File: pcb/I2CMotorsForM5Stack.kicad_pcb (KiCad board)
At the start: 2 copper layers, 54 x 54 mm, 26 parts, among them J1 free_holes, J2 Conn_01x04, J3 Conn_01x06, U1 TB6612FNG, U2 ATmega328P-MU

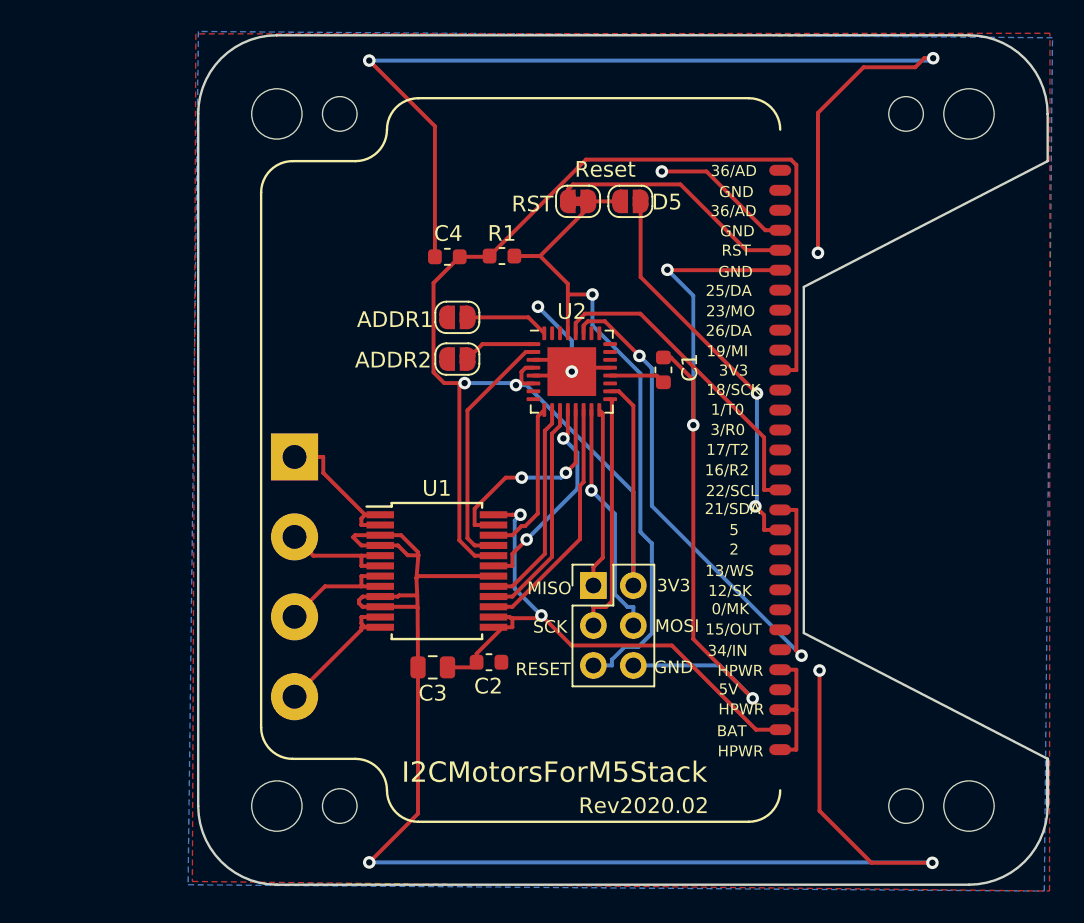
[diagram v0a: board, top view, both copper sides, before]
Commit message: Put terminal mount out side of m5stack zone
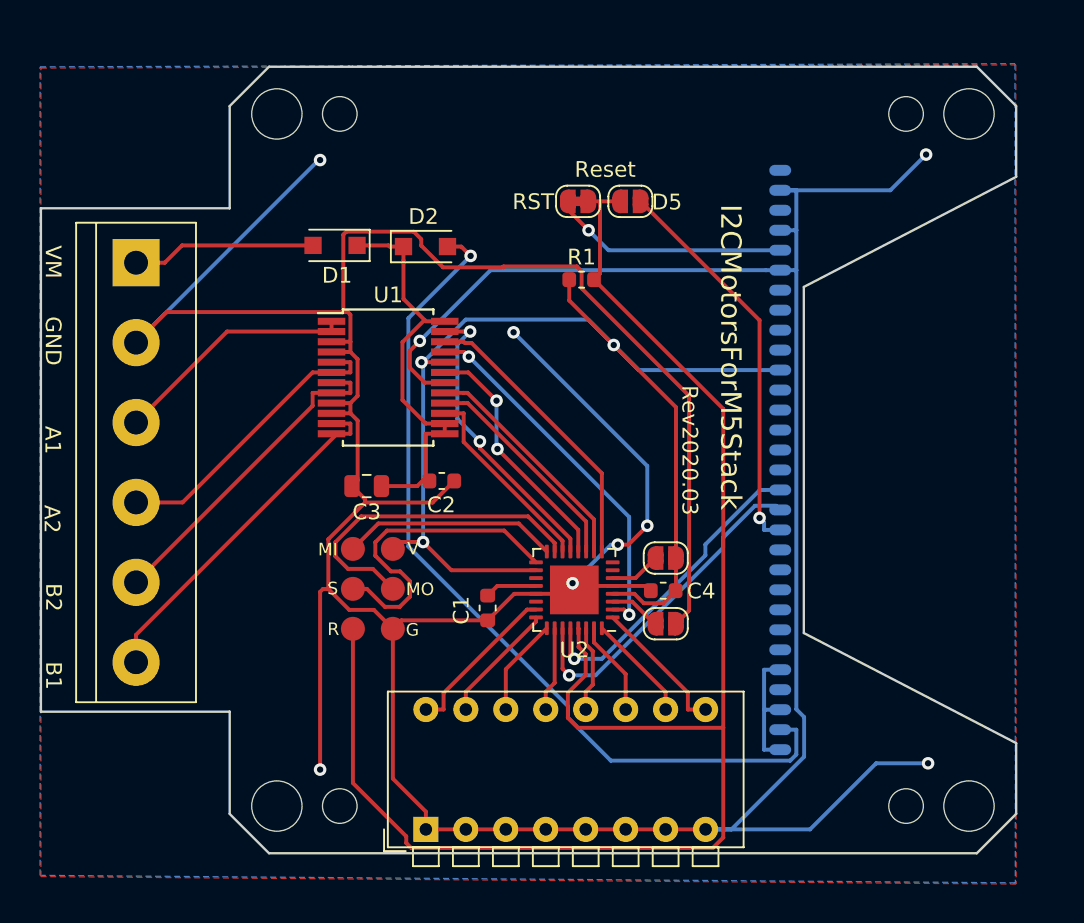
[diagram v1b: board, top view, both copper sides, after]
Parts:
- removed J2: Conn_01x04, TerminalBlock:TerminalBlock_bornier-4_P5.08mm
- removed corner1, corner2, corner3, corner4: outer_corner, footprints:outer_corner
- added D1: D, Diode_SMD:D_SOD-123F, F.Cu at (106.7, 61.4)
- added D2: D, Diode_SMD:D_SOD-123F, F.Cu at (112.4, 61.4)
- added J4: Conn_01x06, TerminalBlock:TerminalBlock_bornier-6_P5.08mm, F.Cu at (94.0, 62.5)
- added SW1: SW_DIP_x08, Button_Switch_THT:SW_DIP_SPSTx08_Piano_CTS_Series194-8MSTN_W7.62mm_P2.54mm, F.Cu at (112.5, 98.5)
- J1: moved to B.Cu
- J3: footprint Connector_PinHeader_2.54mm:PinHeader_2x03_P2.54mm_Vertical -> footprints:2x03_P2.54mm_Pads
- JP3, JP4: value Jumper_NO_Small -> NC
- U2: value ATmega328P-MU -> ATmega328PB-MU
- moved C4 25.3 mm to (127.6, 83.3)
- moved JP3 23.6 mm to (127.7, 85.4)
- moved C1 18.8 mm to (116.4, 84.4), turned to 270 degrees
- moved JP4 18.3 mm to (127.7, 81.2)
- moved J3 14.0 mm to (109.1, 83.2)
- moved U2 13.9 mm to (121.9, 83.3), turned to 180 degrees
- moved U1 12.7 mm to (110.1, 69.8)
- moved C3 12.3 mm to (108.7, 76.7)
- moved C2 11.9 mm to (113.5, 76.3)
- moved R1 5.28 mm to (122.4, 63.5)
- turned J1 to 180 degrees
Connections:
- C2 pad 1: +BATT -> Net-(C2-Pad1)
- C3 pad 1: +BATT -> Net-(C2-Pad1)
- JP3 pad 1: /ADDR1 -> GND
- JP3 pad 2: GND -> Net-(JP3-Pad2)
- JP4 pad 1: /ADDR2 -> +3V3
- JP4 pad 2: GND -> Net-(JP4-Pad2)
- U1 pad 13: +BATT -> Net-(C2-Pad1)
- U1 pad 14: +BATT -> Net-(C2-Pad1)
- U1 pad 24: +BATT -> Net-(C2-Pad1)
- U2 pad 1: /ADDR2 -> /ADDR8
- U2 pad 23: Net-(U2-Pad23) -> /ADDR1
- U2 pad 24: Net-(U2-Pad24) -> /ADDR2
- U2 pad 25: Net-(U2-Pad25) -> /ADDR3
- U2 pad 26: Net-(U2-Pad26) -> /ADDR4
- U2 pad 3: GND -> Net-(JP3-Pad2)
- U2 pad 30: Net-(U2-Pad30) -> /ADDR5
- U2 pad 31: Net-(U2-Pad31) -> /ADDR6
- U2 pad 32: /ADDR1 -> /ADDR7
- U2 pad 6: +3V3 -> Net-(JP4-Pad2)
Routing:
- net GND: track 236.6 -> 300.2 mm, vias 12 -> 9
- net /SPI_RESET: track 43.5 -> 98.1 mm, vias 1 -> 0
- net Net-(C2-Pad1): track 0.00 -> 26.5 mm
- net +3V3: track 96.6 -> 75.4 mm, vias 2 -> 3
- net +BATT: track 37.0 -> 55.3 mm, vias 2 -> 1
- net /21: track 38.8 -> 21.5 mm, vias 2 -> 1
- net /B1: track 9.32 -> 22.9 mm
- net /B2: track 8.10 -> 20.9 mm
- net VCC: track 0.00 -> 11.7 mm
- net /A2: track 7.80 -> 18.9 mm
- net /ADDR8: track 0.00 -> 8.96 mm
- net /AIN2: track 10.1 -> 18.4 mm
- net /AIN1: track 15.7 -> 23.5 mm, vias 0 -> 2
- net /ADDR7: track 0.00 -> 6.85 mm
- net /MOSI: track 15.0 -> 21.3 mm, vias 1 -> 0
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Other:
- board size 54 x 54 mm -> 62 x 50 mm
- board text added: "Please put components on front side."
- board text added: "Rev2020.03"
- board text added: "VM"
- board text removed: "ADDR1"
- board text removed: "ADDR2"
- board text removed: "MISO"
- board text removed: "MOSI"
- board text removed: "Please put components on back side."
- board text removed: "RESET"
- board text removed: "Rev2020.02"
- board text removed: "SCK"

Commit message: Use rounded corner
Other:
- board size 62 x 50 mm -> 60 x 50 mm
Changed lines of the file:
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@@
   (general
     (thickness 1.6)
-    (drawings 59)
+    (drawings 67)
     (tracks 346)
     (zones 0)
@@
     (tags D_SOD-123F)
     (attr smd)
-    (fp_text reference D1 (at -0.127 -1.905) (layer F.SilkS)
+    (fp_text reference D1 (at -0.0248 1.875) (layer F.SilkS)
       (effects (font (size 1 1) (thickness 0.15)))
     )
@@
     )
   )
-  (gr_line (start 100 91) (end 100 97.5) (layer Edge.Cuts) (width 0.15))
-  (gr_line (start 88 91) (end 100 91) (layer Edge.Cuts) (width 0.15))
-  (gr_line (start 88 59) (end 88 91) (layer Edge.Cuts) (width 0.15))
-  (gr_line (start 100 59) (end 88 59) (layer Edge.Cuts) (width 0.15))
-  (gr_text VM (at 88.7738 62.4082 270) (layer F.SilkS)
+  (gr_text B1 (at 90.8988 87.9082 270) (layer B.SilkS)
+    (effects (font (size 1 1) (thickness 0.15)) (justify mirror))
+  )
+  (gr_text B2 (at 90.7738 82.8082 270) (layer B.SilkS)
+    (effects (font (size 1 1) (thickness 0.15)) (justify mirror))
+  )
+  (gr_text A2 (at 90.8488 77.6832 270) (layer B.SilkS)
+    (effects (font (size 1 1) (thickness 0.15)) (justify mirror))
+  )
+  (gr_text A1 (at 90.8488 72.5332 270) (layer B.SilkS)
+    (effects (font (size 1 1) (thickness 0.15)) (justify mirror))
+  )
+  (gr_text GND (at 90.8488 67.5082 270) (layer B.SilkS)
+    (effects (font (size 1 1) (thickness 0.15)) (justify mirror))
+  )
+  (gr_text VM (at 90.8238 62.5082 270) (layer B.SilkS)
+    (effects (font (size 1 1) (thickness 0.15)) (justify mirror))
+  )
+  (gr_arc (start 92 93) (end 90 93) (angle -90) (layer Edge.Cuts) (width 0.15))
+  (gr_arc (start 92 57) (end 92 55) (angle -90) (layer Edge.Cuts) (width 0.15))
+  (gr_line (start 100 95) (end 100 97.5) (layer Edge.Cuts) (width 0.15))
+  (gr_line (start 92 95) (end 100 95) (layer Edge.Cuts) (width 0.15))
+  (gr_line (start 90 57) (end 90 93) (layer Edge.Cuts) (width 0.15))
+  (gr_line (start 100 55) (end 92 55) (layer Edge.Cuts) (width 0.15))
+  (gr_text VM (at 92.6738 55.8582 180) (layer F.SilkS)
     (effects (font (size 1 1) (thickness 0.15)))
   )
-  (gr_text GND (at 88.7738 67.4332 270) (layer F.SilkS)
+  (gr_text GND (at 93.0488 57.4082 180) (layer F.SilkS)
     (effects (font (size 1 1) (thickness 0.15)))
   )
@@
   (gr_line (start 102.5 100) (end 147.5 100) (layer Edge.Cuts) (width 0.15))
   (gr_line (start 100 97.5) (end 102.5 100) (layer Edge.Cuts) (width 0.15))
-  (gr_line (start 100 52.5) (end 100 59) (layer Edge.Cuts) (width 0.15))
+  (gr_line (start 100 52.5) (end 100 55) (layer Edge.Cuts) (width 0.15))
   (gr_line (start 102.5 50) (end 100 52.5) (layer Edge.Cuts) (width 0.15))
   (gr_line (start 147.5 50) (end 102.5 50) (layer Edge.Cuts) (width 0.15))
@@
     (effects (font (size 1 1) (thickness 0.15)))
   )
-  (gr_text B1 (at 88.7988 88.7082 270) (layer F.SilkS)
+  (gr_text B1 (at 92.2488 94.1582) (layer F.SilkS)
     (effects (font (size 1 1) (thickness 0.15)))
   )
-  (gr_text B2 (at 88.7988 83.7332 270) (layer F.SilkS)
+  (gr_text B2 (at 92.2488 92.7332) (layer F.SilkS)
     (effects (font (size 1 1) (thickness 0.15)))
   )
-  (gr_text A2 (at 88.6988 78.7582 270) (layer F.SilkS)
+  (gr_text A2 (at 92.3488 91.3082) (layer F.SilkS)
     (effects (font (size 1 1) (thickness 0.15)))
   )
-  (gr_text A1 (at 88.7488 73.7332 270) (layer F.SilkS)
+  (gr_text A1 (at 92.4488 58.9082 180) (layer F.SilkS)
     (effects (font (size 1 1) (thickness 0.15)))
   )
@@
     (polygon
       (pts
-        (xy 149.9988 101.9582) (xy 87.9988 101.4832) (xy 87.9988 50.0832) (xy 149.9738 49.8832)
+        (xy 149.9988 101.9582) (xy 87.3988 101.556437) (xy 87.3988 50.159963) (xy 149.9738 49.8832)
       )
     )
@@
     (polygon
       (pts
-        (xy 149.9488 101.8832) (xy 87.9488 101.4082) (xy 87.9488 50.0082) (xy 149.9238 49.8082)
+        (xy 149.9488 101.8832) (xy 87.5488 101.3082) (xy 87.5488 49.9082) (xy 149.9238 49.8082)
       )
     )

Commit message: Add diode to connect VM and GND
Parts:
- added D3: D, Diode_SMD:D_SOD-123F, F.Cu at (112.5, 57.6)
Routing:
- net GND: track 300.2 -> 311.0 mm
- net Net-(C2-Pad1): track 26.5 -> 30.3 mm
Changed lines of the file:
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@@
-(kicad_pcb (version 20171130) (host pcbnew 5.1.5-52549c5~84~ubuntu18.04.1)
+(kicad_pcb (version 20171130) (host pcbnew 5.1.5-52549c5~86~ubuntu18.04.1)
   (general
     (thickness 1.6)
     (drawings 67)
-    (tracks 346)
+    (tracks 356)
     (zones 0)
-    (modules 25)
+    (modules 26)
     (nets 59)
   )
@@
     (add_net VCC)
   )
+  (module Diode_SMD:D_SOD-123F (layer F.Cu)
+    (at 112.4738 57.6082)
+    (descr D_SOD-123F)
+    (tags D_SOD-123F)
+    (attr smd)
+    (fp_text reference D3 (at -0.127 -1.905) (layer F.SilkS)
+      (effects (font (size 1 1) (thickness 0.15)))
+    )
+    (fp_text value D (at 0 2.1) (layer F.Fab)
+      (effects (font (size 1 1) (thickness 0.15)))
+    )
+    (fp_line (start -2.2 -1) (end 1.65 -1) (layer F.SilkS) (width 0.12))
+    (fp_line (start -2.2 1) (end 1.65 1) (layer F.SilkS) (width 0.12))
+    (fp_line (start -2.2 -1.15) (end -2.2 1.15) (layer F.CrtYd) (width 0.05))
+    (fp_line (start 2.2 1.15) (end -2.2 1.15) (layer F.CrtYd) (width 0.05))
+    (fp_line (start 2.2 -1.15) (end 2.2 1.15) (layer F.CrtYd) (width 0.05))
+    (fp_line (start -2.2 -1.15) (end 2.2 -1.15) (layer F.CrtYd) (width 0.05))
+    (fp_line (start -1.4 -0.9) (end 1.4 -0.9) (layer F.Fab) (width 0.1))
+    (fp_line (start 1.4 -0.9) (end 1.4 0.9) (layer F.Fab) (width 0.1))
+    (fp_line (start 1.4 0.9) (end -1.4 0.9) (layer F.Fab) (width 0.1))
+    (fp_line (start -1.4 0.9) (end -1.4 -0.9) (layer F.Fab) (width 0.1))
+    (fp_line (start -0.75 0) (end -0.35 0) (layer F.Fab) (width 0.1))
+    (fp_line (start -0.35 0) (end -0.35 -0.55) (layer F.Fab) (width 0.1))
+    (fp_line (start -0.35 0) (end -0.35 0.55) (layer F.Fab) (width 0.1))
+    (fp_line (start -0.35 0) (end 0.25 -0.4) (layer F.Fab) (width 0.1))
+    (fp_line (start 0.25 -0.4) (end 0.25 0.4) (layer F.Fab) (width 0.1))
+    (fp_line (start 0.25 0.4) (end -0.35 0) (layer F.Fab) (width 0.1))
+    (fp_line (start 0.25 0) (end 0.75 0) (layer F.Fab) (width 0.1))
+    (fp_line (start -2.2 -1) (end -2.2 1) (layer F.SilkS) (width 0.12))
+    (fp_text user %R (at -0.127 -1.905) (layer F.Fab)
+      (effects (font (size 1 1) (thickness 0.15)))
+    )
+    (pad 2 smd rect (at 1.4 0) (size 1.1 1.1) (layers F.Cu F.Paste F.Mask)
+      (net 1 GND))
+    (pad 1 smd rect (at -1.4 0) (size 1.1 1.1) (layers F.Cu F.Paste F.Mask)
+      (net 49 "Net-(C2-Pad1)"))
+    (model ${KISYS3DMOD}/Diode_SMD.3dshapes/D_SOD-123F.wrl
+      (at (xyz 0 0 0))
+      (scale (xyz 1 1 1))
+      (rotate (xyz 0 0 0))
+    )
+  )
   (module Package_DFN_QFN:QFN-32-1EP_5x5mm_P0.5mm_EP3.1x3.1mm (layer F.Cu)
     (at 121.911 83.2582 180)
@@
   (gr_line (start 98 97) (end 98 53) (layer Eco1.User) (width 0.15))
   (segment (start 107.2236 65.5975) (end 107.2236 60.6735) (width 0.25) (layer F.Cu) (net 1))
-  (segment (start 107.2236 60.6735) (end 107.4143 60.4828) (width 0.25) (layer F.Cu) (net 1))
-  (segment (start 107.4143 60.4828) (end 111.6988 60.4828) (width 0.25) (layer F.Cu) (net 1))
   (segment (start 111.6988 60.4828) (end 112.1804 60.9644) (width 0.25) (layer F.Cu) (net 1))
   (segment (start 112.1804 60.9644) (end 112.1804 61.3709) (width 0.25) (layer F.Cu) (net 1))
@@
   (segment (start 126.5488 79.1832) (end 126.5488 75.3832) (width 0.25) (layer B.Cu) (net 1))
   (segment (start 126.5488 75.3832) (end 118.0488 66.8832) (width 0.25) (layer B.Cu) (net 1))
+  (segment (start 111.6988 58.9832) (end 113.0738 57.6082) (width 0.25) (layer F.Cu) (net 1))
+  (segment (start 111.6988 60.4828) (end 111.6988 58.9832) (width 0.25) (layer F.Cu) (net 1))
+  (segment (start 113.0738 57.6082) (end 113.8738 57.6082) (width 0.25) (layer F.Cu) (net 1))
+  (segment (start 113.8738 56.8082) (end 113.0488 55.9832) (width 0.25) (layer F.Cu) (net 1))
+  (segment (start 113.8738 57.6082) (end 113.8738 56.8082) (width 0.25) (layer F.Cu) (net 1))
+  (segment (start 113.0488 55.9832) (end 109.4988 55.9832) (width 0.25) (layer F.Cu) (net 1))
+  (segment (start 107.3988 58.0832) (end 107.3988 60.4832) (width 0.25) (layer F.Cu) (net 1))
+  (segment (start 109.4988 55.9832) (end 107.3988 58.0832) (width 0.25) (layer F.Cu) (net 1))
+  (segment (start 107.2236 60.6735) (end 107.3988 60.4832) (width 0.25) (layer F.Cu) (net 1))
+  (segment (start 107.3988 60.4832) (end 107.4143 60.4828) (width 0.25) (layer F.Cu) (net 1))
   (segment (start 115.3185 62.0274) (end 114.7243 61.4332) (width 0.25) (layer F.Cu) (net 2))
   (segment (start 136.0253 92.145) (end 136.0253 93.7234) (width 0.25) (layer B.Cu) (net 2))
@@
   (segment (start 108.099 61.3582) (end 110.0987 61.3582) (width 0.25) (layer F.Cu) (net 49))
   (segment (start 110.0987 61.3582) (end 110.1737 61.4332) (width 0.25) (layer F.Cu) (net 49))
+  (segment (start 111.0738 61.4084) (end 111.049 61.4332) (width 0.25) (layer F.Cu) (net 49))
+  (segment (start 111.0738 57.6082) (end 111.0738 61.4084) (width 0.25) (layer F.Cu) (net 49))
   (segment (start 94.0488 62.4582) (end 95.8741 62.4582) (width 0.25) (layer F.Cu) (net 50))
   (segment (start 105.299 61.3582) (end 96.9741 61.3582) (width 0.25) (layer F.Cu) (net 50))

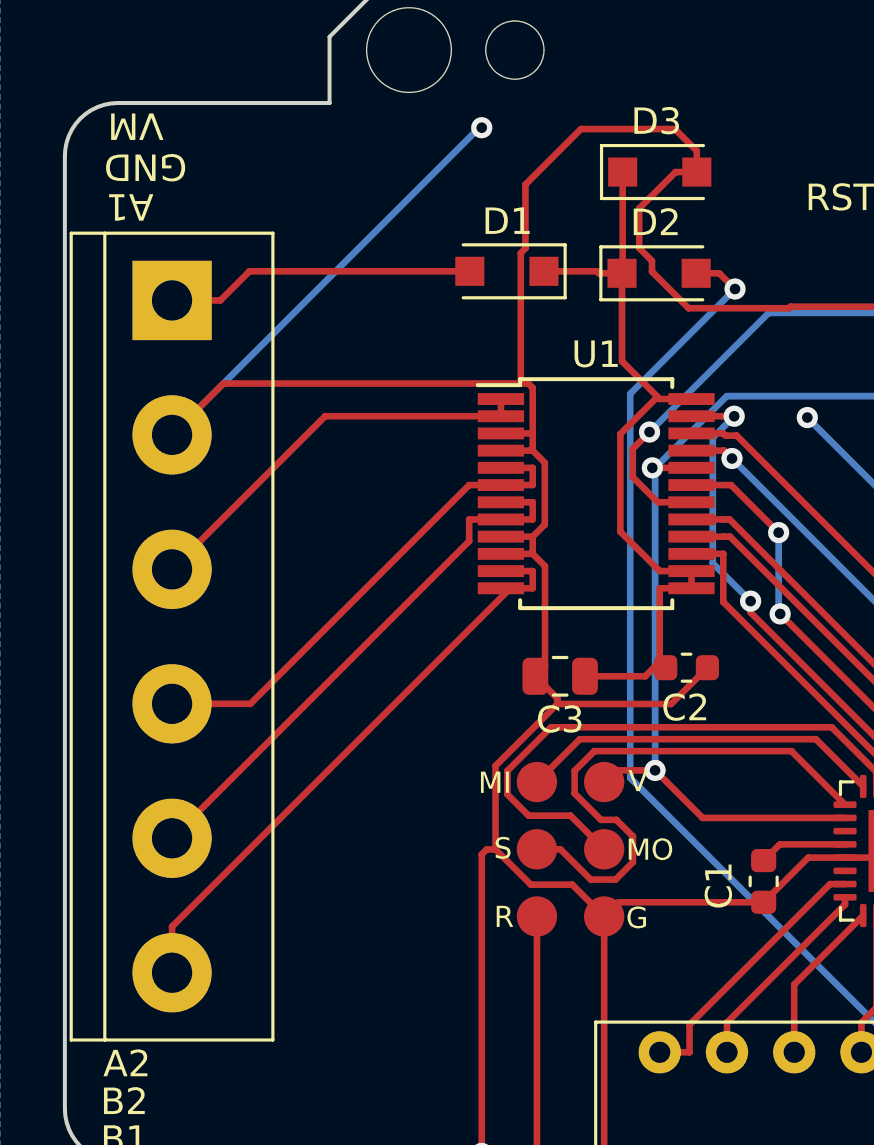
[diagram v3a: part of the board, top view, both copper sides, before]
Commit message: Assign thick line to motor power
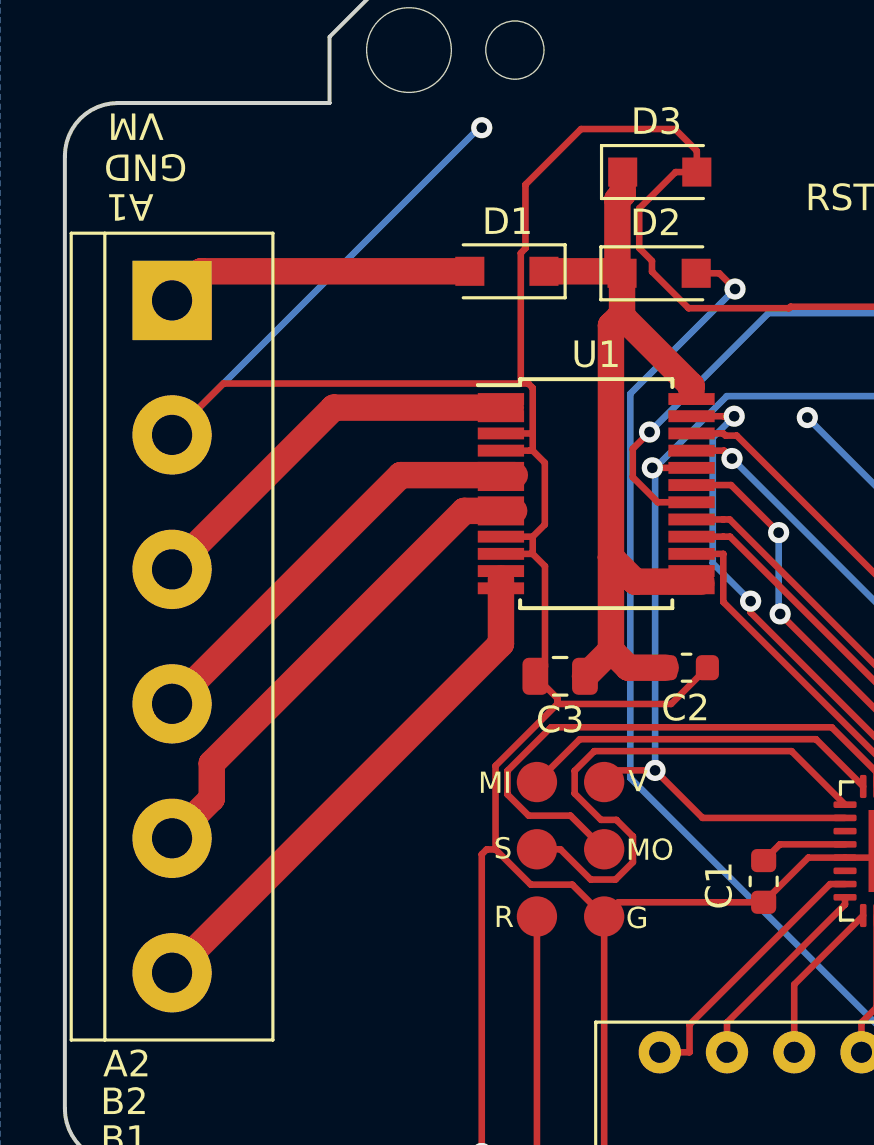
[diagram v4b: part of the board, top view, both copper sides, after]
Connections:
- net Net-(C2-Pad1) renamed /VM
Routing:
- net /VM: track 30.3 -> 33.6 mm
- net /B1: track 22.9 -> 20.0 mm
- net /A2: track 18.9 -> 16.5 mm
- net /B2: track 20.9 -> 18.8 mm
- net /A1: track 15.5 -> 16.0 mm
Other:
- net class MotorPower added: clearance 0.2, trace_width 1, via_dia 0.8, via_drill 0.4
